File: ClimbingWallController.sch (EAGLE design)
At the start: 61 parts, among them IC1 74HCT138D, IC2 74HCT138D, IC3 PIC24FJ32GA004, IC4 4052D, IC5 4052D, Q1 NC, X1 MINI-USB-32005-201

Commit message: Created separate schematics for Row and Column Driver circuits. Added arrayed row and column noise filtering circuits. Added decoupling caps for ICs. Added voltage regulators for 3.3 and 5v rails. Added voltage regulators to parts library. Added values to LED driver current sense resistors.
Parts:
- added C10, C15, C17, C29, C39: 1uF, rcl:C-USC0805
- added C11, C12, C13, C14, C16, C18: 0.1uF, rcl:C-USC0805
- added C19, C21, C30, C40: 100uF, resistor:CPOL-USD
- added C20, C22, C23, C24, C25, C26, C27, C28, C31, C32, C33, C34, C35, C36, C37, C38: 20n, resistor:C-USC0805
- added C41, C42, C43, C44, C45, C46, C47, C48, C49, C50, C51, C52, C53, C54, C55, C56, C57, C58, C59, C60, C61, C62, C63, C64, C65, C66, C67, C68, C69, C70, C71, C72, C73, C74, C75, C76, C77, C78, C79, C80, C81, C82, C83, C84, C85, C86, C87, C88: 1n, resistor:C-USC0805
- added C8: 470pF, rcl:C-USC0805
- added C9: 10uF, rcl:C-USC1206K
- added D1, D10, D11, D12, D13, D14, D15, D16, D17, D18, D19, D2, D20, D21, D22, D23, D24, D25, D26, D27, D28, D29, D3, D30, D31, D32, D33, D34, D35, D36, D37, D38, D39, D4, D40, D41, D42, D43, D44, D45, D46, D47, D48, D49, D5, D50, D51, D52, D53, D54, D55, D56, D57, D58, D59, D6, D60, D61, D62, D63, D64, D7, D8, D9: RB521S30T1G, diode:DIODE-SOD523
- added IC6: TC1015, Parts:TC1015
- added IC7: NCP1117, Parts:NCP1117
- added Q10, Q11, Q12, Q13, Q14, Q15, Q16, Q17, Q2, Q3, Q4, Q5, Q6, Q7, Q8, Q9: PBSS5160U, transistor:-PNP-SOT23-BCE
- added R100, R101, R102, R103, R104, R105, R106, R107, R108, R109, R110, R111, R112, R113, R114, R115, R116, R117, R118, R119, R120, R121, R122, R123, R124, R125, R126, R127, R128, R129, R130, R131, R132, R133, R134, R135, R88, R89, R90, R91, R92, R93, R94, R95, R96, R97, R98, R99: 300, resistor:R-US_R0805
- added R36: 0, resistor:R-US_R0805
- added R37, R38, R39, R42, R45, R48, R51, R54, R57, R60, R63, R66, R69, R72, R75, R78, R81, R84, R87: NC, resistor:R-US_R0805
- added R40, R43, R46, R49, R52, R55, R58, R61, R64, R67, R70, R73, R76, R79, R82, R85: 20, resistor:R-US_R0805
- added R41, R44, R47, R50, R53, R56, R59, R62, R65, R68, R71, R74, R77, R80, R83, R86: 500, resistor:R-US_R0805
- added SG1: NC, buzzer:F/CM04P
- added XTAL1: NC, crystal:CRYSTALHC49UP
- C1: value 10uF Low ESR -> 10uF; device rcl:C-USC0805 -> rcl:C-USC1206K
- Q1: device crystal:CRYSTALHC49UP -> transistor:-NPN-SOT23-EBC
- R7, R8: value Size 1% -> 1.37k 0.5%
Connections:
- new net N$100: C58.1, R105.1
- new net N$101: D35.A, R106.2
- new net N$102: C59.1, R106.1
- new net N$103: D36.A, R107.2
- new net N$104: C60.1, R107.1
- new net N$105: D37.A, R108.2
- new net N$106: C61.1, R108.1
- new net N$107: D38.A, R109.2
- new net N$108: C62.1, R109.1
- new net N$109: D39.A, R110.2
- new net N$110: C63.1, R110.1
- new net N$111: D40.A, R111.2
- new net N$112: C64.1, R111.1
- new net N$113: D41.A, R112.2
- new net N$114: C65.1, R112.1
- new net N$115: D42.A, R113.2
- new net N$116: C66.1, R113.1
- new net N$117: D43.A, R114.2
- new net N$118: C67.1, R114.1
- new net N$119: D44.A, R115.2
- new net N$120: C68.1, R115.1
- new net N$121: D45.A, R116.2
- new net N$122: C69.1, R116.1
- new net N$123: D46.A, R117.2
- new net N$124: C70.1, R117.1
- new net N$125: D47.A, R118.2
- new net N$126: C71.1, R118.1
- new net N$127: D48.A, R119.2
- new net N$128: C72.1, R119.1
- new net N$129: D49.A, R120.2
- new net N$130: C73.1, R120.1
- new net N$131: D50.A, R121.2
- new net N$132: C74.1, R121.1
- new net N$133: D51.A, R122.2
- new net N$134: C75.1, R122.1
- new net N$135: D52.A, R123.2
- new net N$136: C76.1, R123.1
- new net N$137: D53.A, R124.2
- new net N$138: C77.1, R124.1
- new net N$139: D54.A, R125.2
- new net N$140: C78.1, R125.1
- new net N$141: D55.A, R126.2
- new net N$142: C79.1, R126.1
- new net N$143: D56.A, R127.2
- new net N$144: C80.1, R127.1
- new net N$145: D57.A, R128.2
- new net N$146: C81.1, R128.1
- new net N$147: D58.A, R129.2
- new net N$148: C82.1, R129.1
- new net N$149: D59.A, R130.2
- new net N$150: C83.1, R130.1
- new net N$151: D60.A, R131.2
- new net N$152: C84.1, R131.1
- new net N$153: D61.A, R132.2
- new net N$154: C85.1, R132.1
- new net N$155: D62.A, R133.2
- new net N$156: C86.1, R133.1
- new net N$157: D63.A, R134.2
- new net N$158: C87.1, R134.1
- new net N$159: D64.A, R135.2
- new net N$160: C88.1, R135.1
- new net N$29: C8.1, IC6.BYPASS
- new net N$30: R37.1, R38.2
- new net N$31: Q1.B, R39.2
- new net N$32: Q1.C, SG1.2
- new net N$33: Q2.B, R41.2, R42.2
- new net N$34: C20.1, R40.1
- new net N$35: Q3.B, R44.2, R45.2
- new net N$36: C22.1, R43.1
- new net N$37: Q4.B, R47.2, R48.2
- new net N$38: C23.1, R46.1
- new net N$39: Q5.B, R50.2, R51.2
- new net N$40: C24.1, R49.1
- new net N$41: Q6.B, R53.2, R54.2
- new net N$42: C25.1, R52.1
- new net N$43: Q7.B, R56.2, R57.2
- new net N$44: C26.1, R55.1
- new net N$45: Q8.B, R59.2, R60.2
- new net N$46: C27.1, R58.1
- new net N$47: Q9.B, R62.2, R63.2
- new net N$48: C28.1, R61.1
- new net N$49: Q10.B, R65.2, R66.2
- new net N$50: C31.1, R64.1
- new net N$51: Q11.B, R68.2, R69.2
- new net N$52: C32.1, R67.1
- new net N$53: Q12.B, R71.2, R72.2
- new net N$54: C33.1, R70.1
- new net N$55: Q13.B, R74.2, R75.2
- new net N$56: C34.1, R73.1
- new net N$57: Q14.B, R77.2, R78.2
- new net N$58: C35.1, R76.1
- new net N$59: Q15.B, R80.2, R81.2
- new net N$60: C36.1, R79.1
- new net N$61: Q16.B, R83.2, R84.2
- new net N$62: C37.1, R82.1
- new net N$63: Q17.B, R86.2, R87.2
- new net N$64: C38.1, R85.1
- new net N$65: D17.A, R88.2
- new net N$66: C41.1, R88.1
- new net N$67: D18.A, R89.2
- new net N$68: C42.1, R89.1
- new net N$69: D19.A, R90.2
- new net N$70: C43.1, R90.1
- new net N$71: D20.A, R91.2
- new net N$72: C44.1, R91.1
- new net N$73: D21.A, R92.2
- new net N$74: C45.1, R92.1
- new net N$75: D22.A, R93.2
- new net N$76: C46.1, R93.1
- new net N$77: D23.A, R94.2
- new net N$78: C47.1, R94.1
- new net N$79: D24.A, R95.2
- new net N$80: C48.1, R95.1
- new net N$81: D25.A, R96.2
- new net N$82: C49.1, R96.1
- new net N$83: D26.A, R97.2
- new net N$84: C50.1, R97.1
- new net N$85: D27.A, R98.2
- new net N$86: C51.1, R98.1
- new net N$87: D28.A, R99.2
- new net N$88: C52.1, R99.1
- new net N$89: D29.A, R100.2
- new net N$90: C53.1, R100.1
- new net N$91: D30.A, R101.2
- new net N$92: C54.1, R101.1
- new net N$93: D31.A, R102.2
- new net N$94: C55.1, R102.1
- new net N$95: D32.A, R103.2
- new net N$96: C56.1, R103.1
- new net N$97: D33.A, R104.2
- new net N$98: C57.1, R104.1
- new net N$99: D34.A, R105.2
- new net ROW0: D1.C, Q2.C, R40.2, ROW0-1.KL
- new net ROW1: D2.C, Q3.C, R43.2, ROW0-2.KL
- new net ROW10: D11.C, Q12.C, R70.2, ROW1-3.KL
- new net ROW11: D12.C, Q13.C, R73.2, ROW1-4.KL
- new net ROW12: D13.C, Q14.C, R76.2, ROW1-5.KL
- new net ROW13: D14.C, Q15.C, R79.2, ROW1-6.KL
- new net ROW14: D15.C, Q16.C, R82.2, ROW1-7.KL
- new net ROW15: D16.C, Q17.C, R85.2, ROW1-8.KL
- new net ROW2: D3.C, Q4.C, R46.2, ROW0-3.KL
- new net ROW3: D4.C, Q5.C, R49.2, ROW0-4.KL
- new net ROW4: D5.C, Q6.C, R52.2, ROW0-5.KL
- new net ROW5: D6.C, Q7.C, R55.2, ROW0-6.KL
- new net ROW6: D7.C, Q8.C, R58.2, ROW0-7.KL
- new net ROW7: D8.C, Q9.C, R61.2, ROW0-8.KL
- new net ROW8: D9.C, Q10.C, R64.2, ROW1-1.KL
- new net ROW9: D10.C, Q11.C, R67.2, ROW1-2.KL
- new net V+: C19.+, IC7G$1.IN, J1.1, R36.1
- net +3V3: now also C11.1, C12.1, C15.1, C16.1, C17.1, C18.1, C9.1, IC6.VOUT, R37.2
- net +5V: now also C10.1, C13.1, C14.1, C21.+, C29.1, C30.+, C39.1, C40.+, D17.C, D18.C, D19.C, D20.C, D21.C, D22.C, D23.C, D24.C, D25.C, D26.C, D27.C, D28.C, D29.C, D30.C, D31.C, D32.C, D33.C, D34.C, D35.C, D36.C, D37.C, D38.C, D39.C, D40.C, D41.C, D42.C, D43.C, D44.C, D45.C, D46.C, D47.C, D48.C, D49.C, D50.C, D51.C, D52.C, D53.C, D54.C, D55.C, D56.C, D57.C, D58.C, D59.C, D60.C, D61.C, D62.C, D63.C, D64.C, IC6.SHDN_, IC6.VIN, IC7G$1.OUT, Q10.E, Q11.E, Q12.E, Q13.E, Q14.E, Q15.E, Q16.E, Q17.E, Q2.E, Q3.E, Q4.E, Q5.E, Q6.E, Q7.E, Q8.E, Q9.E, R36.2, R42.1, R45.1, R48.1, R51.1, R54.1, R57.1, R60.1, R63.1, R66.1, R69.1, R72.1, R75.1, R78.1, R81.1, R84.1, R87.1, SG1.1; no longer J1.1
- net GND: now also C10.2, C11.2, C12.2, C13.2, C14.2, C15.2, C16.2, C17.2, C18.2, C19.-, C20.2, C21.-, C22.2, C23.2, C24.2, C25.2, C26.2, C27.2, C28.2, C29.2, C30.-, C31.2, C32.2, C33.2, C34.2, C35.2, C36.2, C37.2, C38.2, C39.2, C40.-, C41.2, C42.2, C43.2, C44.2, C45.2, C46.2, C47.2, C48.2, C49.2, C50.2, C51.2, C52.2, C53.2, C54.2, C55.2, C56.2, C57.2, C58.2, C59.2, C60.2, C61.2, C62.2, C63.2, C64.2, C65.2, C66.2, C67.2, C68.2, C69.2, C70.2, C71.2, C72.2, C73.2, C74.2, C75.2, C76.2, C77.2, C78.2, C79.2, C8.2, C80.2, C81.2, C82.2, C83.2, C84.2, C85.2, C86.2, C87.2, C88.2, C9.2, D1.A, D10.A, D11.A, D12.A, D13.A, D14.A, D15.A, D16.A, D2.A, D3.A, D4.A, D5.A, D6.A, D7.A, D8.A, D9.A, IC6.GND, IC7G$1.GND, Q1.E, R38.1
- net OSCI: now also XTAL1.1; no longer Q1.1
- net OSCO: now also XTAL1.2; no longer Q1.2
- net ROW0EN_: now also R41.1; no longer IC1.Y0, ROW0-1.KL
- net ROW10EN_: now also R71.1; no longer IC2.Y2, ROW1-3.KL
- net ROW11EN_: now also R74.1; no longer IC2.Y3, ROW1-4.KL
- net ROW12EN_: now also R77.1; no longer IC2.Y4, ROW1-5.KL
- net ROW13EN_: now also R80.1; no longer IC2.Y5, ROW1-6.KL
- net ROW14EN_: now also R83.1; no longer IC2.Y6, ROW1-7.KL
- net ROW15EN_: now also R86.1; no longer IC2.Y7, ROW1-8.KL
- net ROW1EN_: now also R44.1; no longer IC1.Y1, ROW0-2.KL
- net ROW2EN_: now also R47.1; no longer IC1.Y2, ROW0-3.KL
- net ROW3EN_: now also R50.1; no longer IC1.Y3, ROW0-4.KL
- net ROW4EN_: now also R53.1; no longer IC1.Y4, ROW0-5.KL
- net ROW5EN_: now also R56.1; no longer IC1.Y5, ROW0-6.KL
- net ROW6EN_: now also R59.1; no longer IC1.Y6, ROW0-7.KL
- net ROW7EN_: now also R62.1; no longer IC1.Y7, ROW0-8.KL
- net ROW8EN_: now also R65.1; no longer IC2.Y0, ROW1-1.KL
- net ROW9EN_: now also R68.1; no longer IC2.Y1, ROW1-2.KL
- net VREF+: now also R39.1
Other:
- moved on the sheet: J1, JP1, LED2-1, LED2-10, LED2-11, LED2-12, LED2-2, LED2-3, LED2-4, LED2-5, LED2-6, LED2-7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

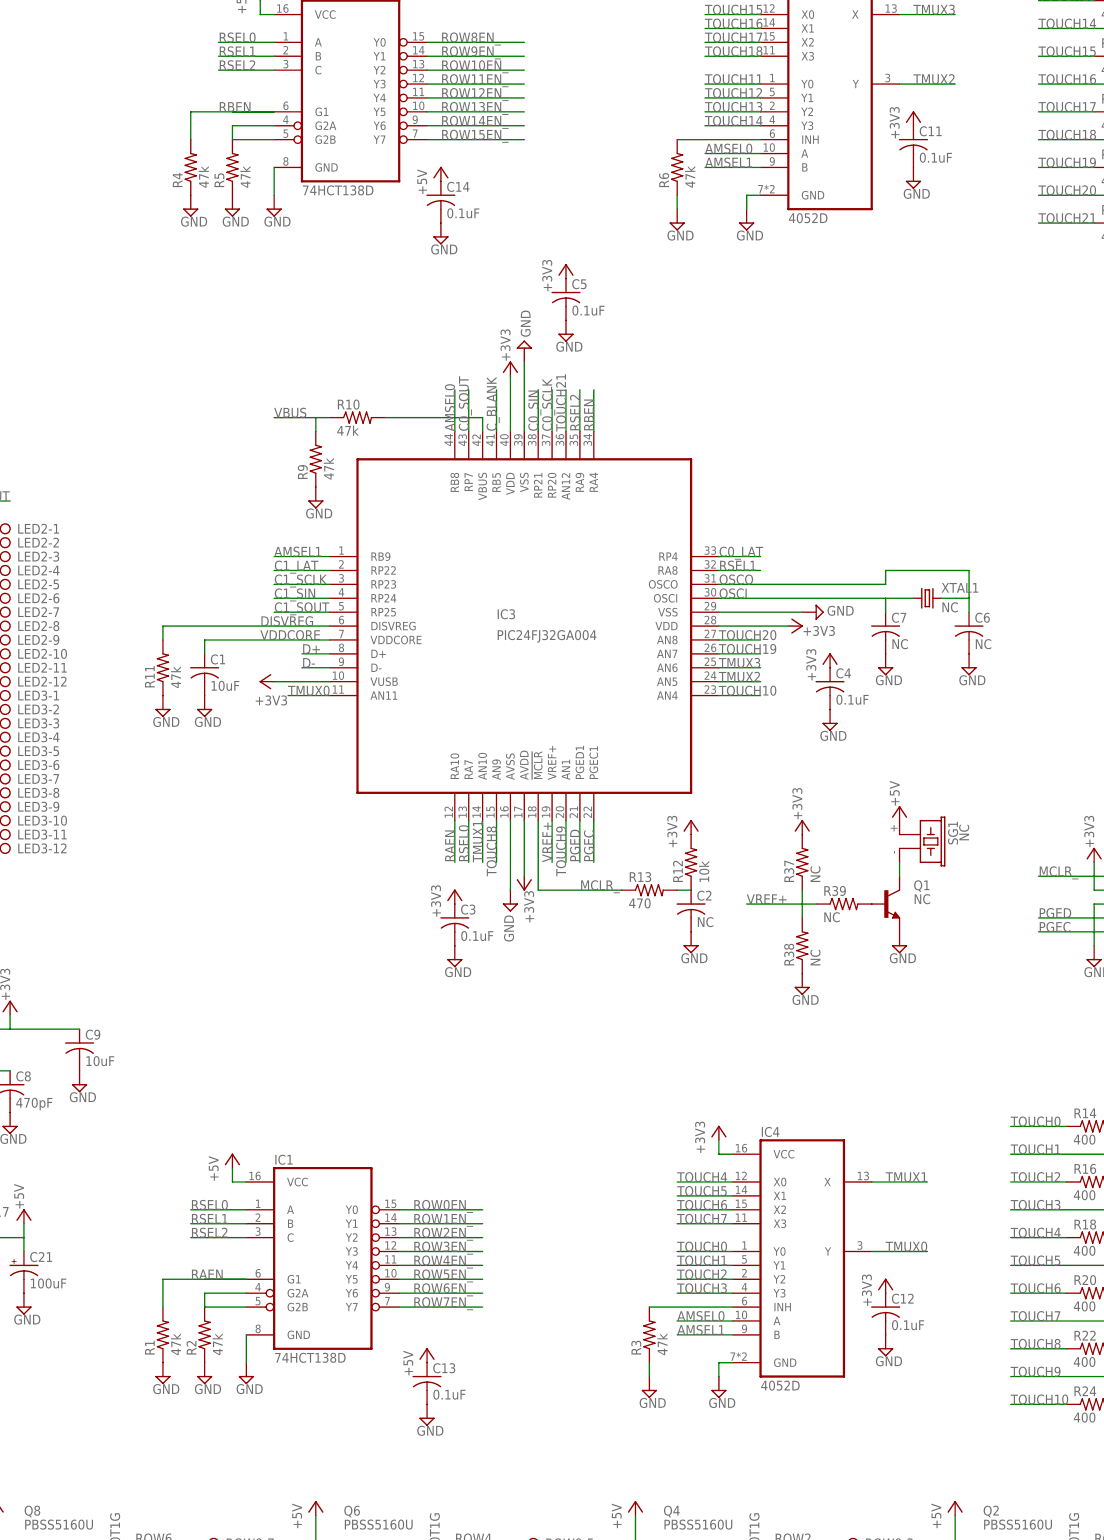
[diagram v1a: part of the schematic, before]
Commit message: Implemented full schematic and filled in component values. Schematic is 95% complete, layout may commence.
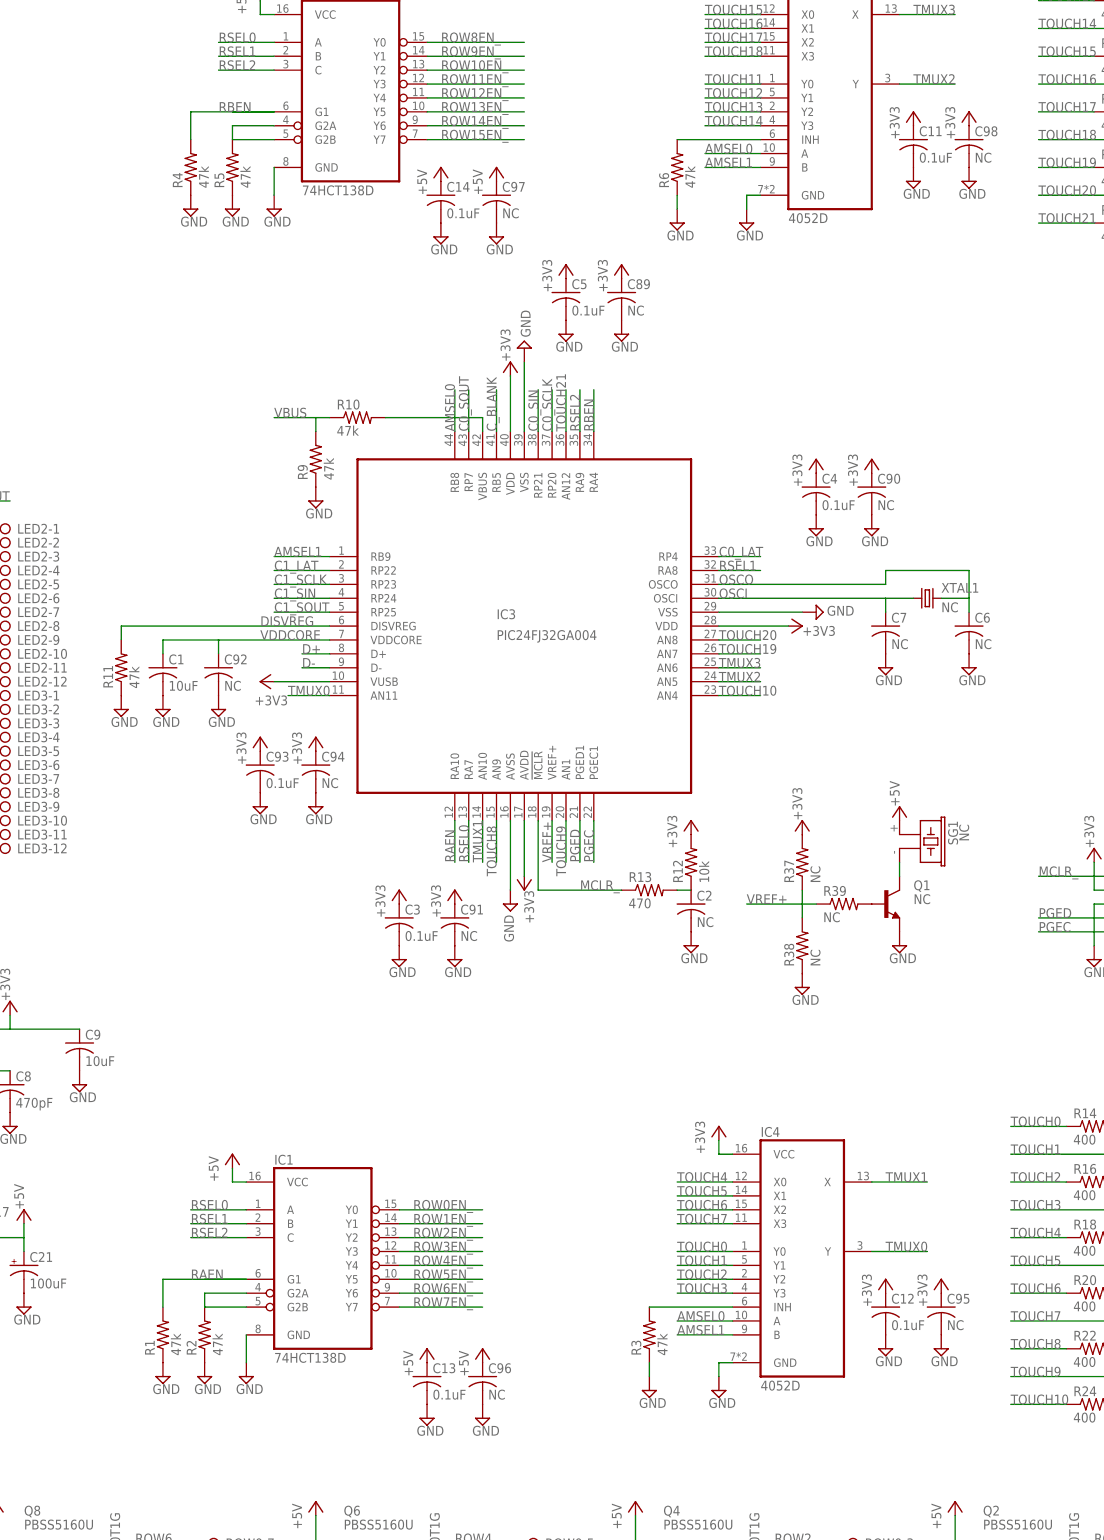
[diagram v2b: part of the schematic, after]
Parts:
- added C89, C90, C91, C92, C94, C95, C96, C97, C98: NC, rcl:C-USC0805
- added C93: 0.1uF, rcl:C-USC0805
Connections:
- net +3V3: now also C89.1, C90.1, C91.1, C93.1, C94.1, C95.1, C98.1
- net +5V: now also C96.1, C97.1
- net GND: now also C89.2, C90.2, C91.2, C92.2, C93.2, C94.2, C95.2, C96.2, C97.2, C98.2
- net VDDCORE: now also C92.1
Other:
- moved on the sheet: C1, C3, C4, R11

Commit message: Cleaned up library further. Picked PNP row switch. Converted placeholder RC values with standard values. Added some part documentation.
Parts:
- removed Q17: PBSS5160U, transistor:-PNP-SOT23-BCE
- added Q18: DPBT8105, Parts:DPBT8105
- C20, C22, C23, C24, C25, C26, C27, C28, C31, C32, C33, C34, C35, C36, C37, C38: value 20n -> 22n
- IC3: value PIC24FJ32GA004 -> PIC24FJ32GB004; device Parts:PIC24FJ32GA004 -> Parts:PIC24FJ32GB004
- IC4, IC5: value 4052D -> SN74LV4052AD; device Parts:4052D -> Parts:SN74LV4052AD
- LED0, LED2: device Parts:W237-12P -> Parts:OSTVN12A150
- Q10, Q11, Q12, Q13, Q14, Q15, Q16, Q2, Q3, Q4, Q5, Q6, Q7, Q8, Q9: value PBSS5160U -> DPBT8105; device transistor:-PNP-SOT23-BCE -> Parts:DPBT8105
- R1, R10, R11, R2, R3, R4, R5, R6, R9: value 47k -> 4.7k
- R12: value 10k -> 4.7k
- R13: value 470 -> 390
- R14, R15, R16, R17, R18, R19, R20, R21, R22, R23, R24, R25, R26, R27, R28, R29, R30, R31, R32, R33, R34, R35: value 400 -> 390
- R41, R44, R47, R50, R53, R56, R59, R62, R65, R68, R71, R74, R77, R80, R83, R86: value 500 -> 750
- ROW0, ROW1: device Parts:W237-08P -> Parts:OSTVN08A150
- TCH0, TCH1: device Parts:W237-11P -> Parts:OSTVN11A150
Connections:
- net +3V3: now also IC3.VDD@1, IC3.VDD@2
- net +5V: now also Q18.E; no longer Q17.E
- net C1_SOUT: now also U$2.SOUT
- net GND: now also IC3.VSS@1, IC3.VSS@2, U$1.EPAD, U$2.EPAD
- net N$49: now also Q18.B; no longer Q10.B
- net N$51: now also Q10.B; no longer Q11.B
- net N$53: now also Q11.B; no longer Q12.B
- net N$55: now also Q12.B; no longer Q13.B
- net N$57: now also Q13.B; no longer Q14.B
- net N$59: now also Q14.B; no longer Q15.B
- net N$61: now also Q15.B; no longer Q16.B
- net N$63: now also Q16.B; no longer Q17.B
- net ROW10: now also Q11.C; no longer Q12.C
- net ROW11: now also Q12.C; no longer Q13.C
- net ROW12: now also Q13.C; no longer Q14.C
- net ROW13: now also Q14.C; no longer Q15.C
- net ROW14: now also Q15.C; no longer Q16.C
- net ROW15: now also Q16.C; no longer Q17.C
- net ROW8: now also Q18.C; no longer Q10.C
- net ROW9: now also Q10.C; no longer Q11.C
- net TMUX0: now also IC3.AN11
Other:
- moved on the sheet: Q10, Q11, Q12, Q13, Q14, Q15, Q16, ROW0-1, ROW0-2, ROW0-3, ROW0-4, ROW0-5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

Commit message: Cleaned up all ERC errors in the schematic.
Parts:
- J1: value (none) -> PWR
- JP1: value (none) -> DEBUG
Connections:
- removed net N$101: D35.A, R106.2
- removed net N$103: D36.A, R107.2
- removed net N$105: D37.A, R108.2
- removed net N$107: D38.A, R109.2
- removed net N$109: D39.A, R110.2
- removed net N$111: D40.A, R111.2
- removed net N$113: D41.A, R112.2
- removed net N$115: D42.A, R113.2
- removed net N$117: D43.A, R114.2
- removed net N$119: D44.A, R115.2
- removed net N$121: D45.A, R116.2
- removed net N$123: D46.A, R117.2
- removed net N$125: D47.A, R118.2
- removed net N$127: D48.A, R119.2
- removed net N$129: D49.A, R120.2
- removed net N$131: D50.A, R121.2
- removed net N$133: D51.A, R122.2
- removed net N$135: D52.A, R123.2
- removed net N$137: D53.A, R124.2
- removed net N$139: D54.A, R125.2
- removed net N$141: D55.A, R126.2
- removed net N$143: D56.A, R127.2
- removed net N$145: D57.A, R128.2
- removed net N$147: D58.A, R129.2
- removed net N$149: D59.A, R130.2
- removed net N$151: D60.A, R131.2
- removed net N$153: D61.A, R132.2
- removed net N$155: D62.A, R133.2
- removed net N$157: D63.A, R134.2
- removed net N$159: D64.A, R135.2
- removed net N$65: D17.A, R88.2
- removed net N$67: D18.A, R89.2
- removed net N$69: D19.A, R90.2
- removed net N$71: D20.A, R91.2
- removed net N$73: D21.A, R92.2
- removed net N$75: D22.A, R93.2
- removed net N$77: D23.A, R94.2
- removed net N$79: D24.A, R95.2
- removed net N$81: D25.A, R96.2
- removed net N$83: D26.A, R97.2
- removed net N$85: D27.A, R98.2
- removed net N$87: D28.A, R99.2
- removed net N$89: D29.A, R100.2
- removed net N$91: D30.A, R101.2
- removed net N$93: D31.A, R102.2
- removed net N$95: D32.A, R103.2
- removed net N$97: D33.A, R104.2
- removed net N$99: D34.A, R105.2
- net B0: now also D19.A, R90.2
- net B1: now also D22.A, R93.2
- net B10: now also D49.A, R120.2
- net B11: now also D52.A, R123.2
- net B12: now also D55.A, R126.2
- net B13: now also D58.A, R129.2
- net B14: now also D61.A, R132.2
- net B15: now also D64.A, R135.2
- net B2: now also D25.A, R96.2
- net B3: now also D28.A, R99.2
- net B4: now also D31.A, R102.2
- net B5: now also D34.A, R105.2
- net B6: now also D37.A, R108.2
- net B7: now also D40.A, R111.2
- net B8: now also D43.A, R114.2
- net B9: now also D46.A, R117.2
- net G0: now also D18.A, R89.2
- net G1: now also D21.A, R92.2
- net G10: now also D48.A, R119.2
- net G11: now also D51.A, R122.2
- net G12: now also D54.A, R125.2
- net G13: now also D57.A, R128.2
- net G14: now also D60.A, R131.2
- net G15: now also D63.A, R134.2
- net G2: now also D24.A, R95.2
- net G3: now also D27.A, R98.2
- net G4: now also D30.A, R101.2
- net G5: now also D33.A, R104.2
- net G6: now also D36.A, R107.2
- net G7: now also D39.A, R110.2
- net G8: now also D42.A, R113.2
- net G9: now also D45.A, R116.2
- net R0: now also D17.A, R88.2
- net R1: now also D20.A, R91.2
- net R10: now also D47.A, R118.2
- net R11: now also D50.A, R121.2
- net R12: now also D53.A, R124.2
- net R13: now also D56.A, R127.2
- net R14: now also D59.A, R130.2
- net R15: now also D62.A, R133.2
- net R2: now also D23.A, R94.2
- net R3: now also D26.A, R97.2
- net R4: now also D29.A, R100.2
- net R5: now also D32.A, R103.2
- net R6: now also D35.A, R106.2
- net R7: now also D38.A, R109.2
- net R8: now also D41.A, R112.2
- net R9: now also D44.A, R115.2
- net ROW0EN_: now also IC1.Y0
- net ROW10EN_: now also IC2.Y2
- net ROW11EN_: now also IC2.Y3
- net ROW12EN_: now also IC2.Y4
- net ROW13EN_: now also IC2.Y5
- net ROW14EN_: now also IC2.Y6
- net ROW15EN_: now also IC2.Y7
- net ROW1EN_: now also IC1.Y1
- net ROW2EN_: now also IC1.Y2
- net ROW3EN_: now also IC1.Y3
- net ROW4EN_: now also IC1.Y4
- net ROW5EN_: now also IC1.Y5
- net ROW6EN_: now also IC1.Y6
- net ROW7EN_: now also IC1.Y7
- net ROW8EN_: now also IC2.Y0
- net ROW9EN_: now also IC2.Y1
- net TOUCH10: now also R24.1
- net TOUCH11: now also R25.1
- net TOUCH13: now also R27.1
- net TOUCH15: now also R29.1
- net TOUCH17: now also R31.1
- net TOUCH2: now also R16.1
- net TOUCH4: now also R18.1
- net TOUCH6: now also R20.1
- net TOUCH8: now also R22.1
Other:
- moved on the sheet: C19, C21

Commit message: Created initial main board. Created layout for row driver, and tiled it. The new board and schematic files for the row driver are intermediate steps.
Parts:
- LED1, LED3: device Parts:W237-12P -> Parts:OSTVN12A150
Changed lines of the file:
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@@
 <part name="SUPPLY14" library="supply2" deviceset="GND" device=""/>
 <part name="LED0" library="Parts" deviceset="OSTVN12A150" device=""/>
-<part name="LED1" library="Parts" deviceset="W237-12P" device=""/>
+<part name="LED1" library="Parts" deviceset="OSTVN12A150" device=""/>
 <part name="LED2" library="Parts" deviceset="OSTVN12A150" device=""/>
-<part name="LED3" library="Parts" deviceset="W237-12P" device=""/>
+<part name="LED3" library="Parts" deviceset="OSTVN12A150" device=""/>
 <part name="X1" library="Parts" deviceset="MINI-USB-" device="32005-201"/>
 <part name="SUPPLY15" library="supply2" deviceset="GND" device=""/>
